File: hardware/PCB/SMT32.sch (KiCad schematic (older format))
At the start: 26 parts, among them J1 47346-0001, J2 1.27mm STDC14, SW1 B3U-1000P, U3 AZ1117CH-3.3TRG1, U4 STM32F303CCT6, Y1 8Mhz 20pf

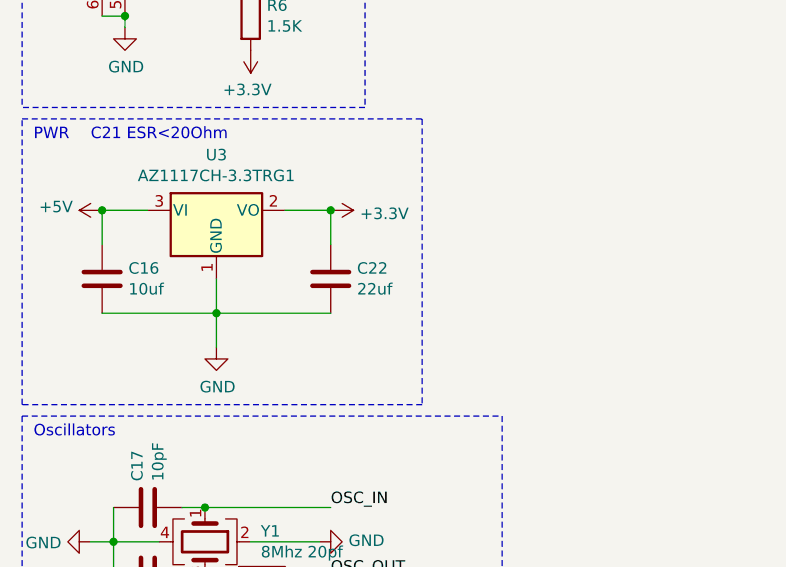
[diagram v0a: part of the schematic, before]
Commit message: I might just have to stick with 1206/4 did some research, maybe time to make another minimal system board....
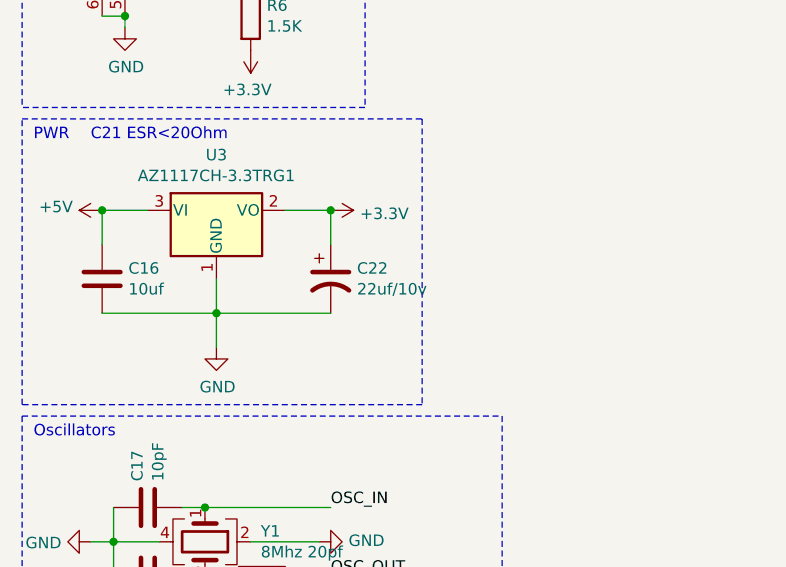
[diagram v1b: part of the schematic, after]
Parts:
- removed C22: 22uf, Capacitor_SMD:C_0603_1608Metric, symbol Device:C
- added C22: 22uf/10v, Capacitor_Tantalum_SMD:CP_EIA-3216-18_Kemet-A, symbol Device:CP1
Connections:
- net +3V3: now also C22.1
- net GND: now also C22.2
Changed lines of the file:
@@
 8Mhz External Crystal\nYou need to change CL capasitors and Resistor\nwhen using a different crystal
-$Comp
-L Device:C C22
-U 1 1 5E352E15
-P 1950 4500
-F 0 "C22" H 2065 4546 50  0000 L CNN
-F 1 "22uf" H 2065 4455 50  0000 L CNN
-F 2 "Capacitor_SMD:C_0603_1608Metric" H 1988 4350 50  0001 C CNN
-F 3 "~" H 1950 4500 50  0001 C CNN
-F 4 "C84419" H 1950 4500 50  0001 C CNN "LCSC"
-F 5 "GRM188R61A226ME15D" H 1950 4500 50  0001 C CNN "Part Number"
-	1    1950 4500
-	1    0    0    -1
-$EndComp
 $Comp
 L Regulator_Linear:AZ1117-3.3 U3
@@
 Text Label 7350 4350 3    50   ~ 0
 D-
+$Comp
+L Device:CP1 C22
+U 1 1 5E47C82C
+P 1950 4500
+F 0 "C22" H 2065 4546 50  0000 L CNN
+F 1 "22uf/10v" H 2065 4455 50  0000 L CNN
+F 2 "Capacitor_Tantalum_SMD:CP_EIA-3216-18_Kemet-A" H 1950 4500 50  0001 C CNN
+F 3 "~" H 1950 4500 50  0001 C CNN
+	1    1950 4500
+	1    0    0    -1
+$EndComp
 $EndSCHEMATC

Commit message: fixing the Tantalum
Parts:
- C22: LCSC (none) -> C11366; Part Number (none) -> TAJA226K010RNJ
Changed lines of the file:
@@
 F 2 "Capacitor_Tantalum_SMD:CP_EIA-3216-18_Kemet-A" H 1950 4500 50  0001 C CNN
 F 3 "~" H 1950 4500 50  0001 C CNN
+F 4 "C11366" H 1950 4500 50  0001 C CNN "LCSC"
+F 5 "TAJA226K010RNJ" H 1950 4500 50  0001 C CNN "Part Number"
 	1    1950 4500
 	1    0    0    -1

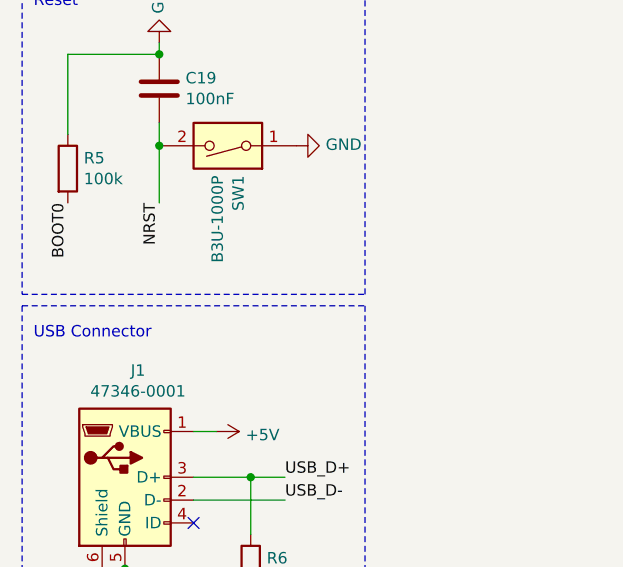
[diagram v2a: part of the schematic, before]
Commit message: Fix the button I can't buy... Change part selections for avalibiliby issues
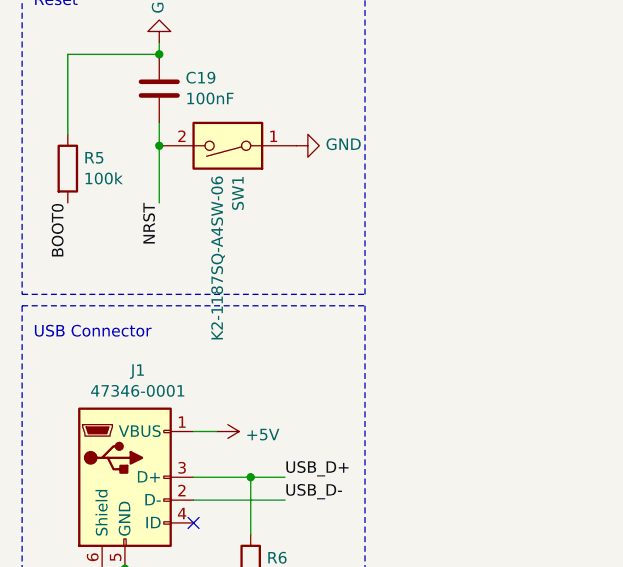
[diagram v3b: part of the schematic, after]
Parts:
- C15, C19, C20, C21, C23: LCSC C24452 -> C307348; Part Number CL10B104JB8NNNC -> CL10B104KB8WPNC
- SW1: value B3U-1000P -> K2-1187SQ-A4SW-06; footprint Button_Switch_SMD:SW_SPST_B3U-1000P -> KiCad:K2-1187SQ-A4SW-06; LCSC C231329 -> C92584; Part Number B3U-1000P -> K2-1187SQ-A4SW-06
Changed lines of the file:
@@
 F 2 "Capacitor_SMD:C_0603_1608Metric" H 2188 6850 50  0001 C CNN
 F 3 "~" H 2150 7000 50  0001 C CNN
-F 4 "C24452" H 2150 7000 50  0001 C CNN "LCSC"
-F 5 "CL10B104JB8NNNC" H 2150 7000 50  0001 C CNN "Part Number"
+F 4 "C307348" H 2150 7000 50  0001 C CNN "LCSC"
+F 5 "CL10B104KB8WPNC" H 2150 7000 50  0001 C CNN "Part Number"
 	1    2150 7000
 	1    0    0    -1
@@
 F 2 "Capacitor_SMD:C_0603_1608Metric" H 1738 6850 50  0001 C CNN
 F 3 "~" H 1700 7000 50  0001 C CNN
-F 4 "C24452" H 1700 7000 50  0001 C CNN "LCSC"
-F 5 "CL10B104JB8NNNC" H 1700 7000 50  0001 C CNN "Part Number"
+F 4 "C307348" H 1700 7000 50  0001 C CNN "LCSC"
+F 5 "CL10B104KB8WPNC" H 1700 7000 50  0001 C CNN "Part Number"
 	1    1700 7000
 	1    0    0    -1
@@
 F 2 "Capacitor_SMD:C_0603_1608Metric" H 1288 6850 50  0001 C CNN
 F 3 "~" H 1250 7000 50  0001 C CNN
-F 4 "C24452" H 1250 7000 50  0001 C CNN "LCSC"
-F 5 "CL10B104JB8NNNC" H 1250 7000 50  0001 C CNN "Part Number"
+F 4 "C307348" H 1250 7000 50  0001 C CNN "LCSC"
+F 5 "CL10B104KB8WPNC" H 1250 7000 50  0001 C CNN "Part Number"
 	1    1250 7000
 	1    0    0    -1
@@
 F 2 "Capacitor_SMD:C_0603_1608Metric" H 838 6850 50  0001 C CNN
 F 3 "~" H 800 7000 50  0001 C CNN
-F 4 "C24452" H 800 7000 50  0001 C CNN "LCSC"
-F 5 "CL10B104JB8NNNC" H 800 7000 50  0001 C CNN "Part Number"
+F 4 "C307348" H 800 7000 50  0001 C CNN "LCSC"
+F 5 "CL10B104KB8WPNC" H 800 7000 50  0001 C CNN "Part Number"
 	1    800  7000
 	1    0    0    -1
@@
 F 2 "Capacitor_SMD:C_0603_1608Metric" H 1238 1100 50  0001 C CNN
 F 3 "~" H 1200 1250 50  0001 C CNN
-F 4 "C24452" H 1200 1250 50  0001 C CNN "LCSC"
-F 5 "CL10B104JB8NNNC" H 1200 1250 50  0001 C CNN "Part Number"
+F 4 "C307348" H 1200 1250 50  0001 C CNN "LCSC"
+F 5 "CL10B104KB8WPNC" H 1200 1250 50  0001 C CNN "Part Number"
 	1    1200 1250
 	1    0    0    -1
@@
 P 1500 1500
 F 0 "SW1" V 1454 1630 50  0000 L CNN
-F 1 "B3U-1000P" V 1545 1630 50  0000 L CNN
-F 2 "Button_Switch_SMD:SW_SPST_B3U-1000P" H 1500 1500 50  0001 C CNN
+F 1 "K2-1187SQ-A4SW-06" V 1545 1630 50  0000 L CNN
+F 2 "KiCad:K2-1187SQ-A4SW-06" H 1500 1500 50  0001 C CNN
 F 3 "https://omronfs.omron.com/en_US/ecb/products/pdf/en-b3u.pdf" H 1500 1500 50  0001 C CNN
-F 4 "B3U-1000P" H 1500 1500 50  0001 C CNN "Part Number"
-F 5 "C231329" H 1500 1500 50  0001 C CNN "LCSC"
+F 4 "K2-1187SQ-A4SW-06" H 1500 1500 50  0001 C CNN "Part Number"
+F 5 "C92584" H 1500 1500 50  0001 C CNN "LCSC"
 	1    1500 1500
 	-1   0    0    1

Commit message: going to make it (prototype!)
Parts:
- C16: LCSC C77040 -> C38898; Part Number GRM188R60J106KE47D -> 0603X106K100NT
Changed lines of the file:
@@
 Sheet 6 6
 Title "NHW68"
-Date "2020-02-10"
-Rev "0.7"
+Date "2020-02-19"
+Rev "0.8"
 Comp ""
 Comment1 ""
@@
 F 2 "Capacitor_SMD:C_0603_1608Metric" H 988 4350 50  0001 C CNN
 F 3 "~" H 950 4500 50  0001 C CNN
-F 4 "C77040" H 950 4500 50  0001 C CNN "LCSC"
-F 5 "GRM188R60J106KE47D" H 950 4500 50  0001 C CNN "Part Number"
+F 4 "C38898" H 950 4500 50  0001 C CNN "LCSC"
+F 5 "0603X106K100NT" H 950 4500 50  0001 C CNN "Part Number"
 	1    950  4500
 	1    0    0    -1

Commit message: Appearently buy parts is hard
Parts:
- C15, C19, C20, C21, C23: LCSC C307348 -> C80516; Part Number CL10B104KB8WPNC -> 0603B104K160CT
- R11, R12, R6, R7: LCSC C114668 -> C103303; Part Number RC0603FR-071K5L -> RTT031501FTP
- R5, R8: LCSC C116674 -> C100703; Part Number AC0603FR-07100KL -> CR0603FA1003G
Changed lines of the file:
@@
 F 2 "Resistor_SMD:R_0603_1608Metric" V 4580 4200 50  0001 C CNN
 F 3 "~" H 4650 4200 50  0001 C CNN
-F 4 "C116674" H 4650 4200 50  0001 C CNN "LCSC"
-F 5 "AC0603FR-07100KL" H 4650 4200 50  0001 C CNN "Part Number"
+F 4 "C100703" H 4650 4200 50  0001 C CNN "LCSC"
+F 5 "CR0603FA1003G" H 4650 4200 50  0001 C CNN "Part Number"
 	1    4650 4200
 	-1   0    0    1
@@
 F 2 "Capacitor_SMD:C_0603_1608Metric" H 2188 6850 50  0001 C CNN
 F 3 "~" H 2150 7000 50  0001 C CNN
-F 4 "C307348" H 2150 7000 50  0001 C CNN "LCSC"
-F 5 "CL10B104KB8WPNC" H 2150 7000 50  0001 C CNN "Part Number"
+F 4 "C80516" H 2150 7000 50  0001 C CNN "LCSC"
+F 5 "0603B104K160CT" H 2150 7000 50  0001 C CNN "Part Number"
 	1    2150 7000
 	1    0    0    -1
@@
 F 2 "Capacitor_SMD:C_0603_1608Metric" H 1738 6850 50  0001 C CNN
 F 3 "~" H 1700 7000 50  0001 C CNN
-F 4 "C307348" H 1700 7000 50  0001 C CNN "LCSC"
-F 5 "CL10B104KB8WPNC" H 1700 7000 50  0001 C CNN "Part Number"
+F 4 "C80516" H 1700 7000 50  0001 C CNN "LCSC"
+F 5 "0603B104K160CT" H 1700 7000 50  0001 C CNN "Part Number"
 	1    1700 7000
 	1    0    0    -1
@@
 F 2 "Capacitor_SMD:C_0603_1608Metric" H 1288 6850 50  0001 C CNN
 F 3 "~" H 1250 7000 50  0001 C CNN
-F 4 "C307348" H 1250 7000 50  0001 C CNN "LCSC"
-F 5 "CL10B104KB8WPNC" H 1250 7000 50  0001 C CNN "Part Number"
+F 4 "C80516" H 1250 7000 50  0001 C CNN "LCSC"
+F 5 "0603B104K160CT" H 1250 7000 50  0001 C CNN "Part Number"
 	1    1250 7000
 	1    0    0    -1
@@
 F 2 "Capacitor_SMD:C_0603_1608Metric" H 838 6850 50  0001 C CNN
 F 3 "~" H 800 7000 50  0001 C CNN
-F 4 "C307348" H 800 7000 50  0001 C CNN "LCSC"
-F 5 "CL10B104KB8WPNC" H 800 7000 50  0001 C CNN "Part Number"
+F 4 "C80516" H 800 7000 50  0001 C CNN "LCSC"
+F 5 "0603B104K160CT" H 800 7000 50  0001 C CNN "Part Number"
 	1    800  7000
 	1    0    0    -1
@@
 F 2 "Capacitor_SMD:C_0603_1608Metric" H 1238 1100 50  0001 C CNN
 F 3 "~" H 1200 1250 50  0001 C CNN
-F 4 "C307348" H 1200 1250 50  0001 C CNN "LCSC"
-F 5 "CL10B104KB8WPNC" H 1200 1250 50  0001 C CNN "Part Number"
+F 4 "C80516" H 1200 1250 50  0001 C CNN "LCSC"
+F 5 "0603B104K160CT" H 1200 1250 50  0001 C CNN "Part Number"
 	1    1200 1250
 	1    0    0    -1
@@
 F 2 "Resistor_SMD:R_0603_1608Metric" V 1530 3350 50  0001 C CNN
 F 3 "~" H 1600 3350 50  0001 C CNN
-F 4 "C114668" H 1600 3350 50  0001 C CNN "LCSC"
-F 5 "RC0603FR-071K5L" H 1600 3350 50  0001 C CNN "Part Number"
+F 4 "C103303" H 1600 3350 50  0001 C CNN "LCSC"
+F 5 "RTT031501FTP" H 1600 3350 50  0001 C CNN "Part Number"
 	1    1600 3350
 	1    0    0    -1
@@
 F 2 "Resistor_SMD:R_0603_1608Metric" V 730 1600 50  0001 C CNN
 F 3 "~" H 800 1600 50  0001 C CNN
-F 4 "C116674" H 800 1600 50  0001 C CNN "LCSC"
-F 5 "AC0603FR-07100KL" H 800 1600 50  0001 C CNN "Part Number"
+F 4 "C100703" H 800 1600 50  0001 C CNN "LCSC"
+F 5 "CR0603FA1003G" H 800 1600 50  0001 C CNN "Part Number"
 	1    800  1600
 	1    0    0    -1
@@
 F 2 "Resistor_SMD:R_0603_1608Metric" V 7580 3700 50  0001 C CNN
 F 3 "~" H 7650 3700 50  0001 C CNN
-F 4 "C114668" H 7650 3700 50  0001 C CNN "LCSC"
-F 5 "RC0603FR-071K5L" H 7650 3700 50  0001 C CNN "Part Number"
+F 4 "C103303" H 7650 3700 50  0001 C CNN "LCSC"
+F 5 "RTT031501FTP" H 7650 3700 50  0001 C CNN "Part Number"
 	1    7650 3700
 	1    0    0    -1
@@
 F 2 "Resistor_SMD:R_0603_1608Metric" V 7580 4100 50  0001 C CNN
 F 3 "~" H 7650 4100 50  0001 C CNN
-F 4 "C114668" H 7650 4100 50  0001 C CNN "LCSC"
-F 5 "RC0603FR-071K5L" H 7650 4100 50  0001 C CNN "Part Number"
+F 4 "C103303" H 7650 4100 50  0001 C CNN "LCSC"
+F 5 "RTT031501FTP" H 7650 4100 50  0001 C CNN "Part Number"
 	1    7650 4100
 	-1   0    0    1
@@
 F 2 "Resistor_SMD:R_0603_1608Metric" V 1580 5800 50  0001 C CNN
 F 3 "~" H 1650 5800 50  0001 C CNN
-F 4 "C114668" H 1650 5800 50  0001 C CNN "LCSC"
-F 5 "RC0603FR-071K5L" H 1650 5800 50  0001 C CNN "Part Number"
+F 4 "C103303" H 1650 5800 50  0001 C CNN "LCSC"
+F 5 "RTT031501FTP" H 1650 5800 50  0001 C CNN "Part Number"
 	1    1650 5800
 	0    1    1    0

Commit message: change footprint
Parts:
- added P?: USB_C_Plug_USB2.0, symbol Connector:USB_C_Plug_USB2.0
- added R?: 1.5K, Resistor_SMD:R_0603_1608Metric, symbol Device:R
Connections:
- net +3V3: now also R?.2
- net +5V: now also P?.A4 (VBUS), P?.A9 (VBUS), P?.B4 (VBUS), P?.B9 (VBUS)
- net GND: now also P?.A1 (GND), P?.A12 (GND), P?.B1 (GND), P?.B12 (GND), P?.S1 (SHIELD)
- net USB_D+: now also P?.A6 (D+), R?.1
- net USB_D-: now also P?.A7 (D-)
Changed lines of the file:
@@
 	1    0    0    -1
 $EndComp
+$Comp
+L Connector:USB_C_Plug_USB2.0 P?
+U 1 1 5E829184
+P 3000 2950
+F 0 "P?" H 3107 3817 50  0000 C CNN
+F 1 "USB_C_Plug_USB2.0" H 3107 3726 50  0000 C CNN
+F 2 "" H 3150 2950 50  0001 C CNN
+F 3 "https://www.usb.org/sites/default/files/documents/usb_type-c.zip" H 3150 2950 50  0001 C CNN
+	1    3000 2950
+	1    0    0    -1
+$EndComp
+Text Label 4000 3050 0    50   ~ 0
+USB_D+
+Text Label 4000 2850 0    50   ~ 0
+USB_D-
+Wire Wire Line
+	3600 3050 3850 3050
+Wire Wire Line
+	3850 3300 3850 3050
+Connection ~ 3850 3050
+Wire Wire Line
+	3850 3050 4000 3050
+Wire Wire Line
+	3600 2850 4000 2850
+$Comp
+L power:+5V #PWR?
+U 1 1 5E86982C
+P 4000 2350
+F 0 "#PWR?" H 4000 2200 50  0001 C CNN
+F 1 "+5V" V 4015 2478 50  0000 L CNN
+F 2 "" H 4000 2350 50  0001 C CNN
+F 3 "" H 4000 2350 50  0001 C CNN
+	1    4000 2350
+	0    1    1    0
+$EndComp
+$Comp
+L power:+3.3V #PWR?
+U 1 1 5E869832
+P 3850 3600
+F 0 "#PWR?" H 3850 3450 50  0001 C CNN
+F 1 "+3.3V" H 3865 3773 50  0000 C CNN
+F 2 "" H 3850 3600 50  0001 C CNN
+F 3 "" H 3850 3600 50  0001 C CNN
+	1    3850 3600
+	-1   0    0    1
+$EndComp
+$Comp
+L Device:R R?
+U 1 1 5E86983A
+P 3850 3450
+F 0 "R?" H 3920 3496 50  0000 L CNN
+F 1 "1.5K" H 3920 3405 50  0000 L CNN
+F 2 "Resistor_SMD:R_0603_1608Metric" V 3780 3450 50  0001 C CNN
+F 3 "~" H 3850 3450 50  0001 C CNN
+F 4 "C103303" H 3850 3450 50  0001 C CNN "LCSC"
+F 5 "RTT031501FTP" H 3850 3450 50  0001 C CNN "Part Number"
+	1    3850 3450
+	1    0    0    -1
+$EndComp
+$Comp
+L power:GND #PWR?
+U 1 1 5E8A3ECC
+P 3000 4000
+F 0 "#PWR?" H 3000 3750 50  0001 C CNN
+F 1 "GND" H 3005 3827 50  0000 C CNN
+F 2 "" H 3000 4000 50  0001 C CNN
+F 3 "" H 3000 4000 50  0001 C CNN
+	1    3000 4000
+	1    0    0    -1
+$EndComp
+Wire Wire Line
+	3000 4000 3000 3850
+Wire Wire Line
+	2700 3850 3000 3850
+Connection ~ 3000 3850
+Wire Wire Line
+	4000 2350 3600 2350
 $EndSCHEMATC

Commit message: change stuff so everything export the right way
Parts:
- removed P?: USB_C_Plug_USB2.0, symbol Connector:USB_C_Plug_USB2.0
- removed R?: 1.5K, Resistor_SMD:R_0603_1608Metric, symbol Device:R
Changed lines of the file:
@@
 Sheet 6 6
 Title "NHW68"
-Date "2020-02-19"
-Rev "0.8"
+Date "2020-04-05"
+Rev "1.0"
 Comp ""
 Comment1 ""
@@
 	1    0    0    -1
 $EndComp
-$Comp
-L Connector:USB_C_Plug_USB2.0 P?
-U 1 1 5E829184
-P 3000 2950
-F 0 "P?" H 3107 3817 50  0000 C CNN
-F 1 "USB_C_Plug_USB2.0" H 3107 3726 50  0000 C CNN
-F 2 "" H 3150 2950 50  0001 C CNN
-F 3 "https://www.usb.org/sites/default/files/documents/usb_type-c.zip" H 3150 2950 50  0001 C CNN
-	1    3000 2950
-	1    0    0    -1
-$EndComp
-Text Label 4000 3050 0    50   ~ 0
-USB_D+
-Text Label 4000 2850 0    50   ~ 0
-USB_D-
-Wire Wire Line
-	3600 3050 3850 3050
-Wire Wire Line
-	3850 3300 3850 3050
-Connection ~ 3850 3050
-Wire Wire Line
-	3850 3050 4000 3050
-Wire Wire Line
-	3600 2850 4000 2850
-$Comp
-L power:+5V #PWR?
-U 1 1 5E86982C
-P 4000 2350
-F 0 "#PWR?" H 4000 2200 50  0001 C CNN
-F 1 "+5V" V 4015 2478 50  0000 L CNN
-F 2 "" H 4000 2350 50  0001 C CNN
-F 3 "" H 4000 2350 50  0001 C CNN
-	1    4000 2350
-	0    1    1    0
-$EndComp
-$Comp
-L power:+3.3V #PWR?
-U 1 1 5E869832
-P 3850 3600
-F 0 "#PWR?" H 3850 3450 50  0001 C CNN
-F 1 "+3.3V" H 3865 3773 50  0000 C CNN
-F 2 "" H 3850 3600 50  0001 C CNN
-F 3 "" H 3850 3600 50  0001 C CNN
-	1    3850 3600
-	-1   0    0    1
-$EndComp
-$Comp
-L Device:R R?
-U 1 1 5E86983A
-P 3850 3450
-F 0 "R?" H 3920 3496 50  0000 L CNN
-F 1 "1.5K" H 3920 3405 50  0000 L CNN
-F 2 "Resistor_SMD:R_0603_1608Metric" V 3780 3450 50  0001 C CNN
-F 3 "~" H 3850 3450 50  0001 C CNN
-F 4 "C103303" H 3850 3450 50  0001 C CNN "LCSC"
-F 5 "RTT031501FTP" H 3850 3450 50  0001 C CNN "Part Number"
-	1    3850 3450
-	1    0    0    -1
-$EndComp
-$Comp
-L power:GND #PWR?
-U 1 1 5E8A3ECC
-P 3000 4000
-F 0 "#PWR?" H 3000 3750 50  0001 C CNN
-F 1 "GND" H 3005 3827 50  0000 C CNN
-F 2 "" H 3000 4000 50  0001 C CNN
-F 3 "" H 3000 4000 50  0001 C CNN
-	1    3000 4000
-	1    0    0    -1
-$EndComp
-Wire Wire Line
-	3000 4000 3000 3850
-Wire Wire Line
-	2700 3850 3000 3850
-Connection ~ 3000 3850
-Wire Wire Line
-	4000 2350 3600 2350
 $EndSCHEMATC

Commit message: fix some detail for 1.0
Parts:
- added SW1: K2-1187SQ-A4SW-06, KiCad:K2-1187SQ-A4SW-06, symbol Switch:SW_DIP_x01
- renumbered C19 to C17, C16 to C18, C22 to C19, C17 to C20, C18 to C21, C15 to C22, C20 to C23, C21 to C24, C23 to C25, C24 to C26, C25 to C27, C26 to C28, R9 to R10, R10 to R11, R7 to R12, R11 to R7, R12 to R8, R8 to R9, SW1 to SW2, U4 to U3, U3 to U4
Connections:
- net +3V3: now also SW1.1
- net BOOT0: now also SW1.2
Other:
- moved on the sheet: C17, R5, SW2
